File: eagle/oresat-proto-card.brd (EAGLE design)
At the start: 99.8 x 94.7 mm, 113 parts, among them J1 J-SAMTEC-TFM-110-X1-XXX-D-RA, J2 U.FL, J3 U.FL, J4 U.FL, J6 J-SAMTEC-TFM-120-X1-XXX-D-RA, J7 FTSH-105-XX-X-DV-K, Q1 DMP2240UDM, Q3 MOSFET-PCH-SOT23-6, Q4 MOSFET-PCH-SOT23-6, Q5 PMV45EN, Q6 PMV45EN, U2 TCAN330, U3 MAX7310ATE, U4 MAX4211CETE, U5 TPS62111RSA, U6 STM32F042K6, U7 MCP1703A, X1 16MHZ-2.5x2mm

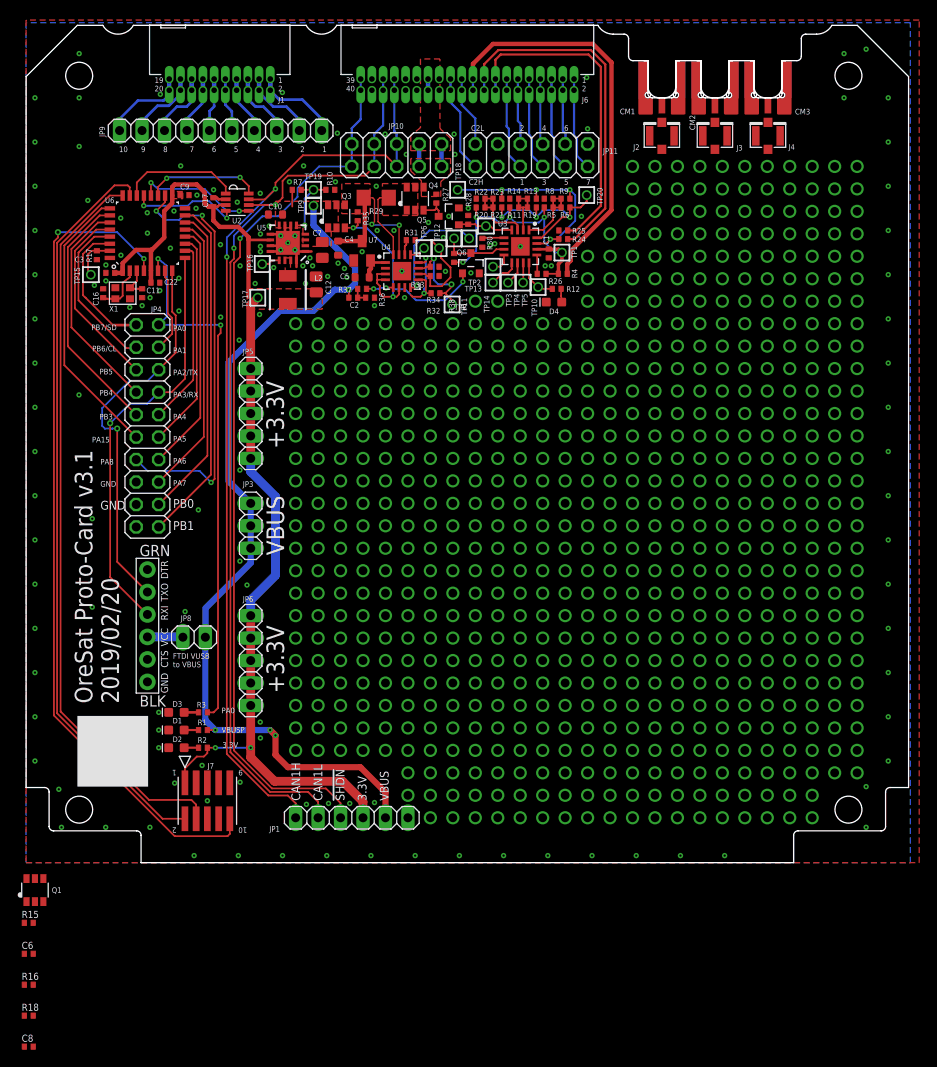
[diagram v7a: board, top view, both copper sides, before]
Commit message: updated m0 protocard to include I2C breaker CAD and added more stitching
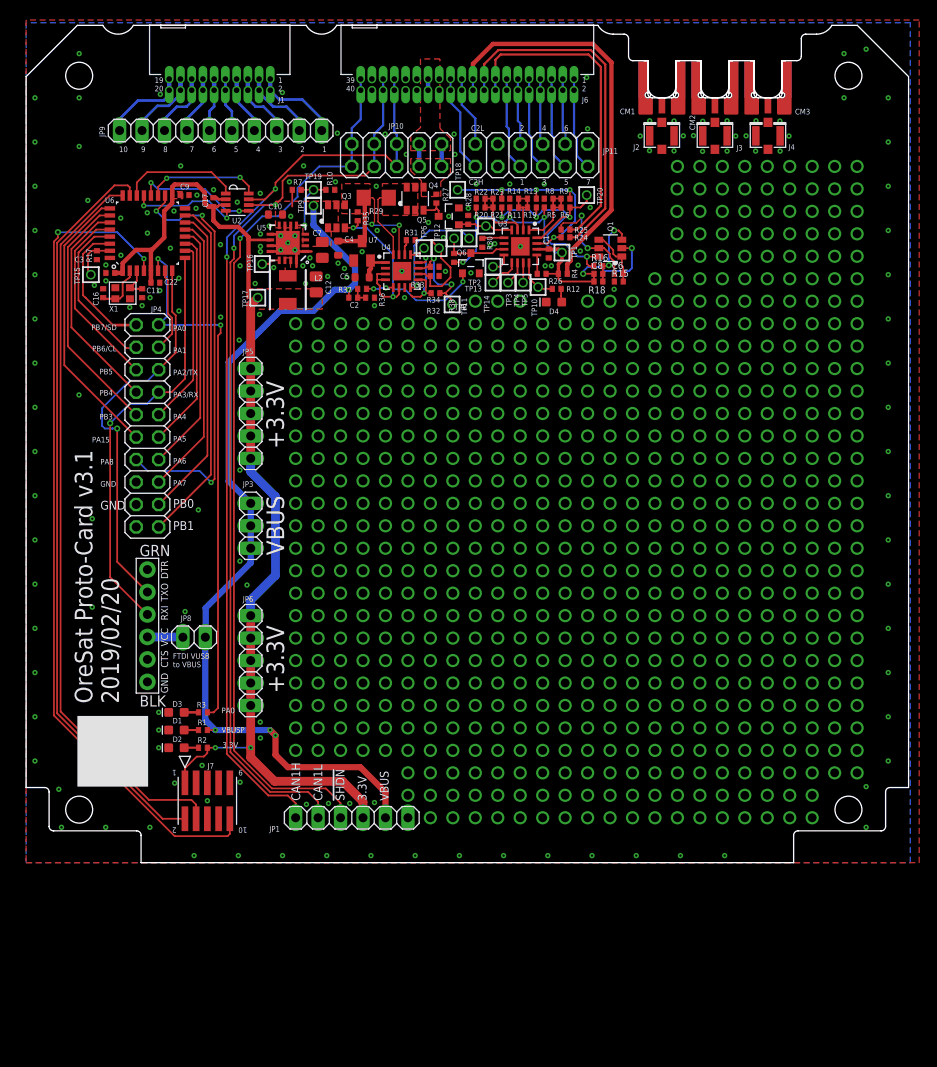
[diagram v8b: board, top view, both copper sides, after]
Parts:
- moved C8 108.6 mm to (64.7, 66.6)
- moved R18 105.1 mm to (64.7, 65.7), turned to 180 degrees
- moved R16 103.7 mm to (64.7, 67.5)
- moved C6 101.8 mm to (67.0, 66.6)
- moved R15 98.5 mm to (67.0, 65.7)
- moved Q1 97.5 mm to (66.1, 69.5), turned to 90 degrees
- moved R24 0.32 mm to (61.0, 70.7)
- moved R25 0.27 mm to (61.0, 71.6)
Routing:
- net VPD: track 31.4 -> 47.9 mm, vias 4 -> 6
- net N$579: track 0.00 -> 12.6 mm, vias 0 -> 2
- net PEN-SDA-FILT: track 20.0 -> 32.2 mm, vias 3 -> 4
- net N$581: track 0.00 -> 8.39 mm, vias 0 -> 2
- net N$580: track 0.00 -> 6.54 mm
- net GND: vias 252 -> 286
